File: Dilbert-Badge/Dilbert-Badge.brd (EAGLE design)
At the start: 100 x 80 mm, 17 parts, among them J1 I2C, J2 UART, SW1 UP, SW2 DOWN, SW3 LEFT, SW4 RIGHT, SW5 A, SW6 B, SW7 RESET

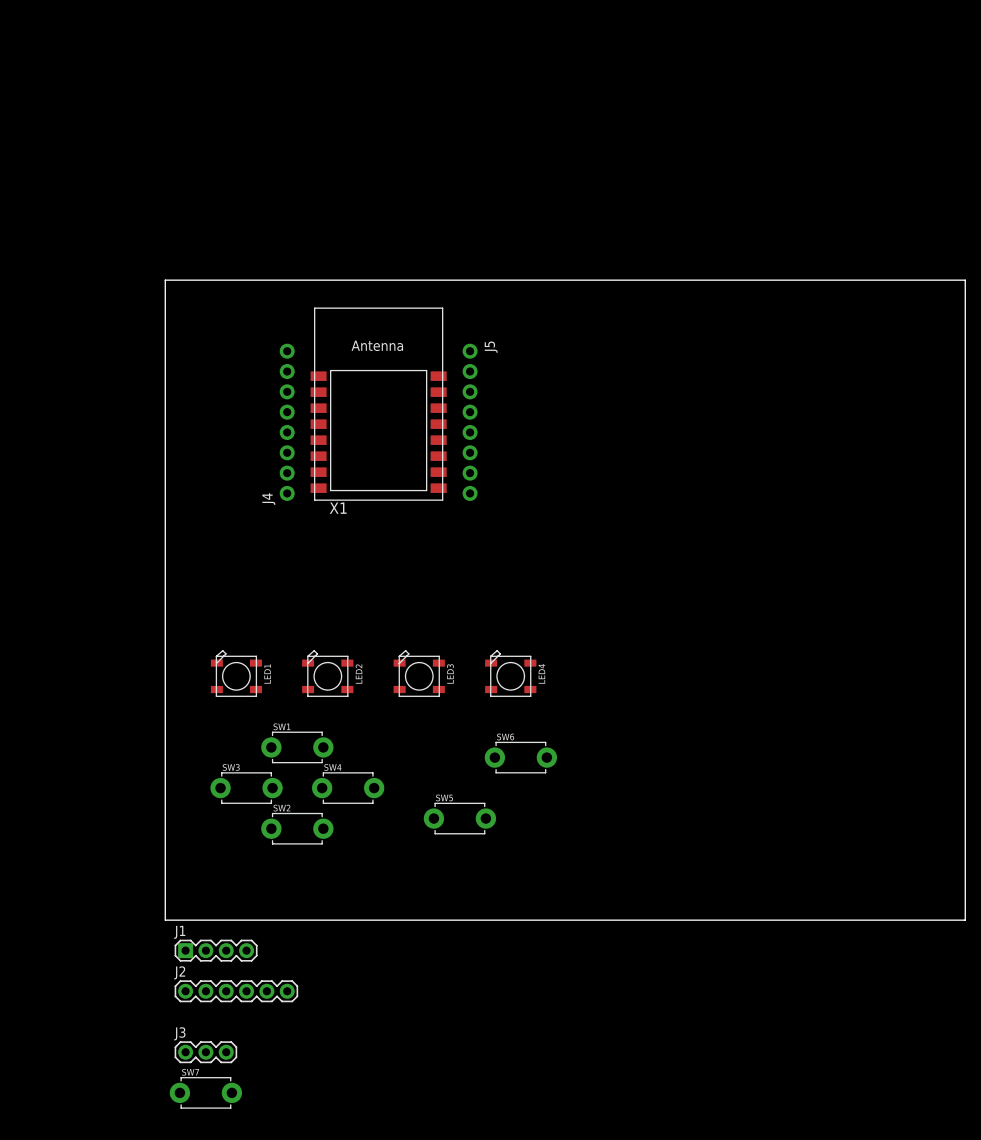
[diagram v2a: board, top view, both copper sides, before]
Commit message: add IO expander, more general layout
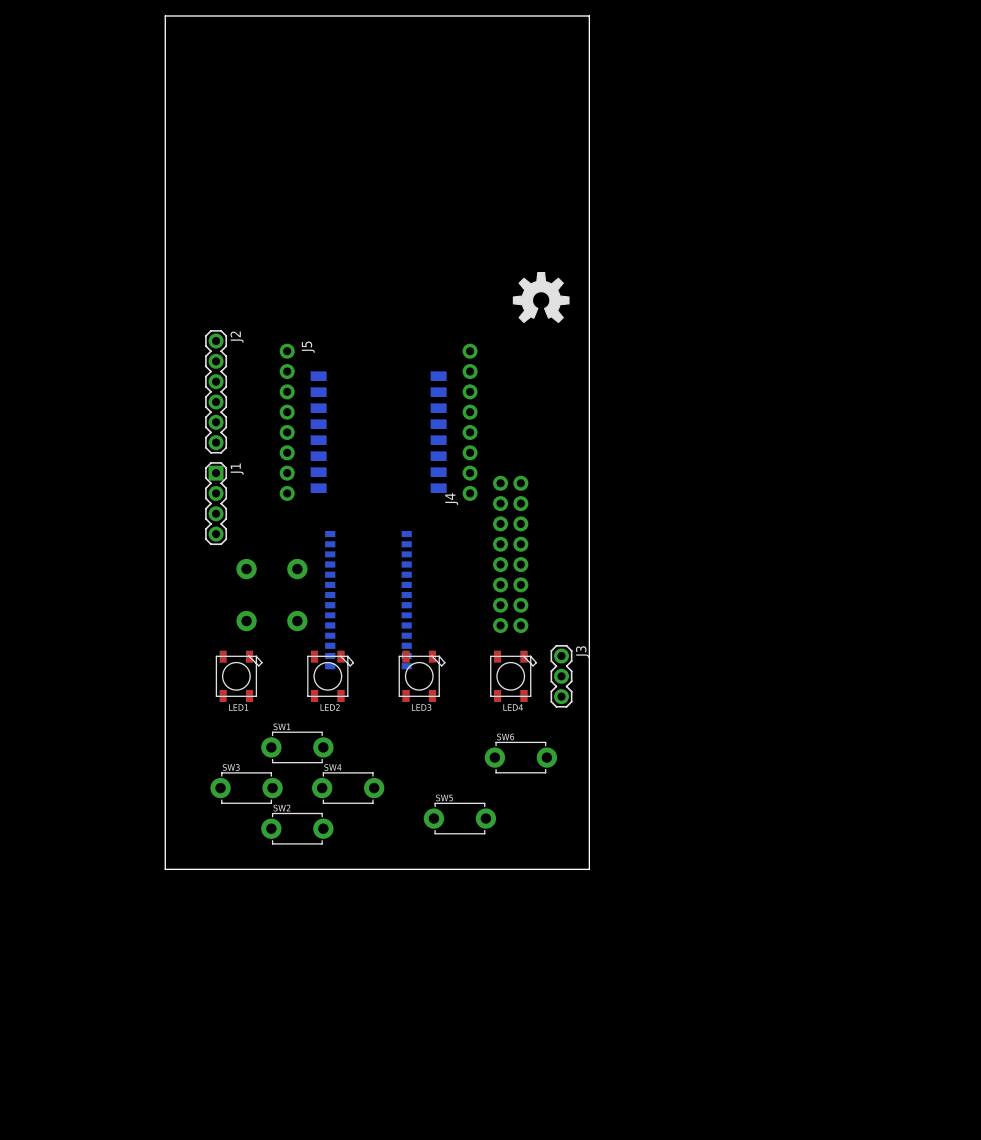
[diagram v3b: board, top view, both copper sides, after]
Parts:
- added IC1: MCP23017SO, adafruit:SO28W
- added J6: IO_B, SparkFun-Connectors:1X08_ROUND
- added J7: IO_A, SparkFun-Connectors:1X08_ROUND
- added LOGO1: OSHW-LOGOL, SparkFun-Aesthetics:OSHW-LOGO-L
- added SW8: SWD, adafruit:TACT_PANA-EVQ
- moved J2 81.4 mm to (6.35, 72.4), turned to 270 degrees
- moved J3 68.3 mm to (49.5, 33.0), turned to 270 degrees
- moved SW7 63.3 mm to (16.5, 40.6), flipped to the bottom, turned to 270 degrees
- moved J1 59.8 mm to (6.35, 55.9), turned to 270 degrees
- moved J4 22.9 mm to (38.1, 53.3)
- moved J5 22.9 mm to (15.2, 71.1)
- turned LED1 to 270 degrees
- turned LED2 to 270 degrees
- turned LED3 to 270 degrees
- turned LED4 to 270 degrees
- flipped X1 to the bottom
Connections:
- removed net N$5: LED1.1-VDD, LED2.1-VDD, LED3.1-VDD, LED4.1-VDD
- new net N$14: IC1.1, J6.1
- new net N$15: IC1.2, J6.2
- new net N$16: IC1.8, J6.8
- new net N$17: IC1.7, J6.7
- new net N$18: IC1.6, J6.6
- new net N$19: IC1.5, J6.5
- new net N$20: IC1.4, J6.4
- new net N$21: IC1.3, J6.3
- new net N$22: IC1.28, J7.8
- new net N$23: IC1.27, J7.7
- new net RESET: J4.8, SW7.P$2, X1.1
- net BTN_A: now also IC1.25, J7.5
- net BTN_B: now also IC1.26, J7.6
- net BTN_D: now also IC1.22, J7.2
- net BTN_L: now also IC1.23, J7.3
- net BTN_R: now also IC1.24, J7.4
- net BTN_U: now also IC1.21, J7.1
- net GND: now also IC1.10, SW8.P$1
- net N$8: now also SW8.P$2; no longer J4.8, X1.1
- net SCL: now also IC1.12
- net SDA: now also IC1.13
- net VCC: now also IC1.9, LED1.1-VDD, LED2.1-VDD, LED3.1-VDD, LED4.1-VDD
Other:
- board size 100 x 80 mm -> 53 x 106.7 mm

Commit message: add puller resistors and decouping
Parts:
- added C1: (no value), SparkFun-Capacitors:0805-CAP
- added R1, R2, R3: 10K, adafruit:R0805
- added R4: (no value), adafruit:R0805
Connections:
- net N$4 renamed ESP_ADC
- removed net N$13: J5.6, X1.11
- removed net N$6: J4.6, X1.3
- removed net N$8: SW8.P$2
- removed net VCC: IC1.9, J1.2, J2.4, J3.2, J4.1, LED1.1-VDD, LED2.1-VDD, LED3.1-VDD, LED4.1-VDD, X1.8
- new net 3V3: C1.1, IC1.9, J1.2, J2.4, J3.2, J4.1, LED1.1-VDD, LED2.1-VDD, LED3.1-VDD, LED4.1-VDD, R1.2, R2.2, R3.2, X1.8
- new net ESP_CH_PD: J4.6, R2.1, X1.3
- new net GPIO2: J5.6, R3.1, X1.11
- net GND: now also C1.2, R4.1
- net LED_IN: now also R4.2
- net RESET: now also R1.1
- net SCL: now also SW8.P$2
